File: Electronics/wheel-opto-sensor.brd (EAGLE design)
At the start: 68.6 x 53.3 mm, 24 parts, among them IC1 BD6230F, IC2 BD6230F, IC3 TS5A23157

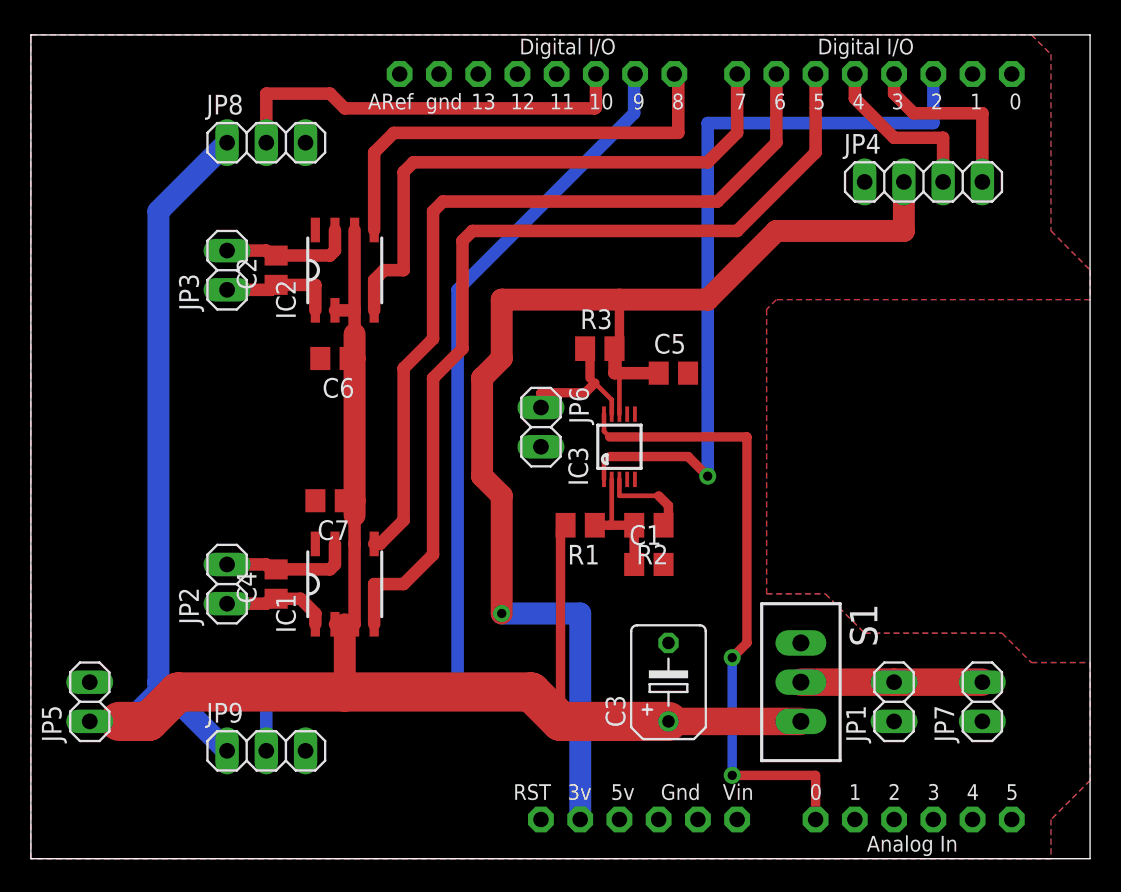
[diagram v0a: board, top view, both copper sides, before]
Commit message: Updated electronics to power the wheel sensors directly off the battery. (They take too much current from 3V3 if that is used; the sensors now have potential dividers so their output never exceeds 3v3.)
Added a PCB test program for the Wemos D1/ESP8266 board (W.I.P.)
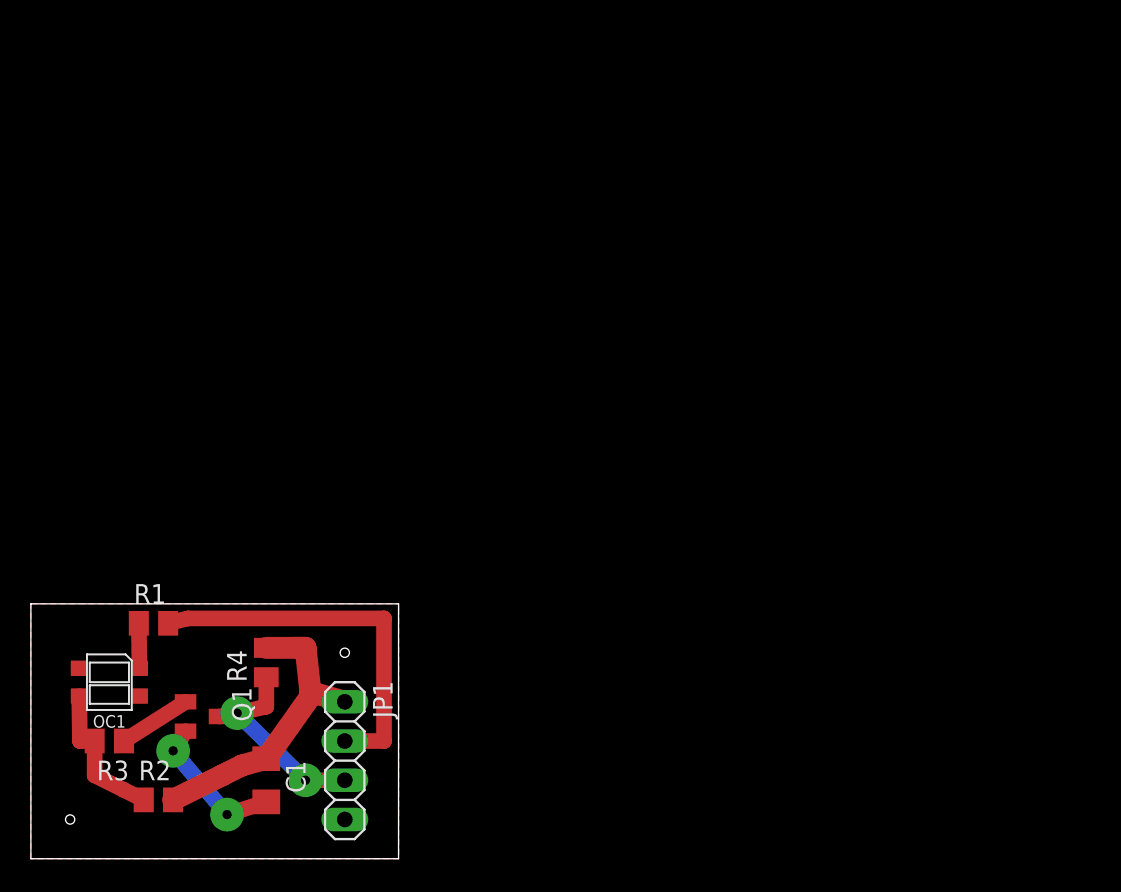
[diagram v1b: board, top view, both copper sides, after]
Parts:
- removed C2, C4, C5, C6, C7: 0.1uF, rcl:C0805
- removed C3: 1000uF, rcl:B45181B
- removed IC1, IC2: BD6230F, rohm:SOP8
- removed IC3: TS5A23157, reprapltd:MSOP10
- removed JP2, JP3, JP5, JP6, JP7: (no value), pinhead:1X02
- removed JP4: (no value), pinhead:1X04
- removed JP8, JP9: (no value), pinhead:1X03
- removed S1: TL36PO, switch:TL3XPO
- removed U$1: ARDUINO-BPLACE, adafruit:ARDUINO-BPLACE
- added OC1: QRE1113GR, we-opto:SMT_GULLWING_4
- added Q1: (no value), adafruit:SOT23
- added R4: 1K, rcl:M0805
- C1: value 1uF -> 10uF; device rcl:C0805 -> rcl:C1206
- JP1: device pinhead:1X02 -> pinhead:1X04
- R1: value 15K -> 100R
- R2: value 10K -> 1K
- R3: value 15K -> 10K
- moved R3 40.7 mm to (5.08, 7.62), turned to 180 degrees
- moved R2 36.4 mm to (8.26, 3.81), turned to 0 degrees
- moved JP1 35.8 mm to (20.3, 6.35), turned to 270 degrees
- moved C1 28.4 mm to (15.2, 5.08), turned to 270 degrees
- moved R1 28.3 mm to (7.94, 15.2), turned to 0 degrees
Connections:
- removed net 5V: U$1.5V
- removed net N$10: IC2.5, U$1.D8
- removed net N$11: IC3.10, U$1.A0
- removed net N$12: C1.1, IC3.2, R1.1, R2.2
- removed net N$13: JP1.2, JP7.2, S1.2
- removed net N$14: IC3.9, JP6.1, R3.1
- removed net N$15: IC3.1, U$1.D2
- removed net N$17: JP9.2, U$1.D9
- removed net N$18: JP8.2, U$1.D10
- removed net N$6: C4.2, IC1.7, JP2.2
- removed net N$7: IC1.5, U$1.D6
- removed net N$8: IC1.4, U$1.D5
- removed net N$9: IC2.4, U$1.D7
- removed net NC2: IC3.7
- removed net V+: C3.+, C6.1, C7.1, IC1.2, IC1.3, IC1.6, IC2.2, IC2.3, IC2.6, JP5.1, JP8.1, JP9.1, R1.2, S1.3
- removed net VIN: U$1.VIN
- net +3V3: now also C1.1, JP1.1, R2.2, R4.2; no longer C5.1, IC3.8, JP4.2, R3.2, U$1.3V
- net GND: now also JP1.4, OC1.2, OC1.4, Q1.2; no longer C3.-, C5.2, C6.2, C7.2, IC1.8, IC2.8, IC3.3, JP1.1, JP4.1, JP5.2, JP6.2, JP7.1, JP8.3, JP9.3, R2.1, U$1.GND, U$1.GND1, U$1.GND2
- net N$1: now also JP1.3, Q1.3, R4.1; no longer JP4.4, U$1.D3
- net N$2: now also OC1.1, R1.1; no longer JP4.3, U$1.D4
- net N$3: now also JP1.2, R1.2; no longer C2.1, IC2.1, JP3.1
- net N$4: now also Q1.1, R3.1; no longer C2.2, IC2.7, JP3.2
- net N$5: now also OC1.3, R2.1, R3.2; no longer C4.1, IC1.1, JP2.1
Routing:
- net V+: track 143.0 -> 0.00 mm
- net +3V3: track 83.2 -> 19.6 mm, vias 1 -> 0
- net N$17: track 60.4 -> 0.00 mm
- net N$8: track 58.6 -> 0.00 mm
- net N$7: track 51.8 -> 0.00 mm
- net N$15: track 49.1 -> 0.00 mm, vias 1 -> 0
- net N$11: track 41.1 -> 0.00 mm, vias 2 -> 0
- net N$9: track 36.9 -> 0.00 mm
- net N$10: track 29.1 -> 0.00 mm
- net N$18: track 27.1 -> 0.00 mm
- net N$3: track 7.50 -> 24.5 mm
- net N$13: track 11.7 -> 0.00 mm
- net N$14: track 9.66 -> 0.00 mm
- net N$6: track 8.58 -> 0.00 mm
- net N$2: track 11.2 -> 2.91 mm
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- removed copper zone on layer 16, net GND
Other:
- board size 68.6 x 53.3 mm -> 23.8 x 16.5 mm
- board text removed: "+"
- board text removed: "+3V3"
- board text removed: "-"
- board text removed: "Batt"
- board text removed: "C"
- board text removed: "E"
- board text removed: "EPS8266/Arduino Shield V1.0 reprapltd.com Mechanics & software: Sally Bowyer Electronics: Adrian Bowyer Licence - GPL"
- board text removed: "Frank The Robot"
- board text removed: "G"
- board text removed: "L. sense"
- board text removed: "LIDAR"
- board text removed: "Left Motor"
- board text removed: "Pwr"
- board text removed: "R. sense"
- board text removed: "Right Motor"
- board text removed: "SCL"
- board text removed: "SDA"
- board text removed: "charge"
- board text removed: "photo"
- board text removed: "sig"
